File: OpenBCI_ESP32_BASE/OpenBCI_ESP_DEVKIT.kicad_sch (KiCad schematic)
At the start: 8 parts, among them J4 Conn_02x08_Odd_Even, U1 LIS3DH, U2 ESP32-DevKitC

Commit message: Firmware updates
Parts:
- added R3, R4: 4k7, Resistor_SMD:R_0603_1608Metric, symbol Device:R
- added R5: 220k, Resistor_SMD:R_0603_1608Metric, symbol Device:R
- added R6: 120k, Resistor_SMD:R_0603_1608Metric, symbol Device:R
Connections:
- net +3V3: now also R3.1, R4.1
- net +5V: now also R5.1
- net GND: now also R6.2
- net SCL: now also R4.2
- net SDA: now also R3.2
- net BATT: no longer names the net of U2.3 (SENSOR_VP/GPIO36/ADC1_CH0)
- net BATT: now also R5.2, R6.1
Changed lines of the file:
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@@
 (kicad_sch (version 20211123) (generator eeschema)
   (paper "A4")
+  (junction (at 68.58 57.15) (diameter 0) (color 0 0 0 0)
+  )
+  (junction (at 85.09 123.19) (diameter 0) (color 0 0 0 0)
+  )
   (junction (at 243.205 56.515) (diameter 0) (color 0 0 0 0)
   )
@@
   (junction (at 128.905 120.65) (diameter 0) (color 0 0 0 0)
   )
+  (junction (at 88.9 138.43) (diameter 0) (color 0 0 0 0)
+  )
   (junction (at 146.05 135.89) (diameter 0) (color 0 0 0 0)
+  )
+  (junction (at 82.55 135.89) (diameter 0) (color 0 0 0 0)
   )
   (no_connect (at 167.64 97.79))
@@
     (stroke (width 0) (type default) (color 0 0 0 0))
   )
+  (wire (pts (xy 68.58 67.31) (xy 68.58 71.12))
+    (stroke (width 0) (type default) (color 0 0 0 0))
+  )
   (wire (pts (xy 142.24 130.81) (xy 146.05 130.81))
     (stroke (width 0) (type default) (color 0 0 0 0))
@@
     (stroke (width 0) (type default) (color 0 0 0 0))
   )
+  (wire (pts (xy 85.09 120.65) (xy 85.09 123.19))
+    (stroke (width 0) (type default) (color 0 0 0 0))
+  )
   (wire (pts (xy 188.595 52.07) (xy 188.595 54.61))
     (stroke (width 0) (type default) (color 0 0 0 0))
   )
+  (wire (pts (xy 85.09 123.19) (xy 88.9 123.19))
+    (stroke (width 0) (type default) (color 0 0 0 0))
+  )
   (wire (pts (xy 213.36 74.93) (xy 223.52 74.93))
     (stroke (width 0) (type default) (color 0 0 0 0))
@@
     (stroke (width 0) (type default) (color 0 0 0 0))
   )
+  (wire (pts (xy 82.55 135.89) (xy 73.66 135.89))
+    (stroke (width 0) (type default) (color 0 0 0 0))
+  )
   (wire (pts (xy 86.36 77.47) (xy 97.79 77.47))
     (stroke (width 0) (type default) (color 0 0 0 0))
   )
+  (wire (pts (xy 88.9 132.08) (xy 88.9 138.43))
+    (stroke (width 0) (type default) (color 0 0 0 0))
+  )
   (wire (pts (xy 236.22 69.85) (xy 245.11 69.85))
     (stroke (width 0) (type default) (color 0 0 0 0))
@@
     (stroke (width 0) (type default) (color 0 0 0 0))
   )
+  (wire (pts (xy 88.9 123.19) (xy 88.9 124.46))
+    (stroke (width 0) (type default) (color 0 0 0 0))
+  )
   (wire (pts (xy 146.05 135.89) (xy 146.05 140.97))
     (stroke (width 0) (type default) (color 0 0 0 0))
@@
     (stroke (width 0) (type default) (color 0 0 0 0))
   )
-  (wire (pts (xy 97.79 57.15) (xy 85.09 57.15))
-    (stroke (width 0) (type default) (color 0 0 0 0))
-  )
   (wire (pts (xy 97.79 82.55) (xy 86.36 82.55))
     (stroke (width 0) (type default) (color 0 0 0 0))
@@
     (stroke (width 0) (type default) (color 0 0 0 0))
   )
-  (wire (pts (xy 116.84 135.89) (xy 98.425 135.89))
+  (wire (pts (xy 116.84 135.89) (xy 82.55 135.89))
     (stroke (width 0) (type default) (color 0 0 0 0))
   )
@@
     (stroke (width 0) (type default) (color 0 0 0 0))
   )
+  (wire (pts (xy 85.09 123.19) (xy 82.55 123.19))
+    (stroke (width 0) (type default) (color 0 0 0 0))
+  )
   (wire (pts (xy 241.3 80.01) (xy 241.3 81.915))
     (stroke (width 0) (type default) (color 0 0 0 0))
@@
     (stroke (width 0) (type default) (color 0 0 0 0))
   )
+  (wire (pts (xy 88.9 138.43) (xy 73.66 138.43))
+    (stroke (width 0) (type default) (color 0 0 0 0))
+  )
   (wire (pts (xy 129.54 148.59) (xy 129.54 156.21))
     (stroke (width 0) (type default) (color 0 0 0 0))
@@
     (stroke (width 0) (type default) (color 0 0 0 0))
   )
+  (wire (pts (xy 82.55 132.08) (xy 82.55 135.89))
+    (stroke (width 0) (type default) (color 0 0 0 0))
+  )
+  (wire (pts (xy 68.58 44.45) (xy 68.58 46.99))
+    (stroke (width 0) (type default) (color 0 0 0 0))
+  )
   (wire (pts (xy 225.425 111.125) (xy 225.425 110.49))
     (stroke (width 0) (type default) (color 0 0 0 0))
@@
     (stroke (width 0) (type default) (color 0 0 0 0))
   )
+  (wire (pts (xy 82.55 123.19) (xy 82.55 124.46))
+    (stroke (width 0) (type default) (color 0 0 0 0))
+  )
   (wire (pts (xy 201.295 140.335) (xy 192.405 140.335))
     (stroke (width 0) (type default) (color 0 0 0 0))
@@
     (stroke (width 0) (type default) (color 0 0 0 0))
   )
-  (wire (pts (xy 116.84 138.43) (xy 98.425 138.43))
+  (wire (pts (xy 68.58 57.15) (xy 68.58 59.69))
+    (stroke (width 0) (type default) (color 0 0 0 0))
+  )
+  (wire (pts (xy 68.58 54.61) (xy 68.58 57.15))
+    (stroke (width 0) (type default) (color 0 0 0 0))
+  )
+  (wire (pts (xy 68.58 57.15) (xy 97.79 57.15))
+    (stroke (width 0) (type default) (color 0 0 0 0))
+  )
+  (wire (pts (xy 116.84 138.43) (xy 88.9 138.43))
     (stroke (width 0) (type default) (color 0 0 0 0))
   )
@@
     (effects (font (size 1.27 1.27)) (justify right bottom))
   )
-  (label "BATT" (at 85.09 57.15 0)
-    (effects (font (size 1.27 1.27)) (justify left bottom))
-  )
   (label "SDCLK" (at 191.77 117.475 0)
     (effects (font (size 1.27 1.27)) (justify left bottom))
@@
     (effects (font (size 1.27 1.27)) (justify left bottom))
   )
-  (label "SCL" (at 98.425 138.43 0)
-    (effects (font (size 1.27 1.27)) (justify left bottom))
-  )
-  (label "SDA" (at 98.425 135.89 0)
+  (label "SCL" (at 73.66 138.43 0)
+    (effects (font (size 1.27 1.27)) (justify left bottom))
+  )
+  (label "SDA" (at 73.66 135.89 0)
     (effects (font (size 1.27 1.27)) (justify left bottom))
   )
@@
     (pin "1")
   )
+  (symbol (lib_id "Device:R") (at 88.9 128.27 0) (unit 1)
+    (in_bom yes) (on_board yes) (fields_autoplaced)
+    (property "Reference" "R4" (id 0) (at 90.678 127.3615 0)
+      (effects (font (size 1.27 1.27)) (justify left))
+    )
+    (property "Value" "4k7" (id 1) (at 90.678 130.1366 0)
+      (effects (font (size 1.27 1.27)) (justify left))
+    )
+    (property "Footprint" "Resistor_SMD:R_0603_1608Metric" (id 2) (at 87.122 128.27 90)
+      (effects (font (size 1.27 1.27)) hide)
+    )
+    (property "Datasheet" "~" (id 3) (at 88.9 128.27 0)
+      (effects (font (size 1.27 1.27)) hide)
+    )
+    (pin "1")
+    (pin "2")
+  )
+  (symbol (lib_id "power:+3.3V") (at 85.09 120.65 0) (unit 1)
+    (in_bom yes) (on_board yes)
+    (property "Reference" "#PWR0116" (id 0) (at 85.09 124.46 0)
+      (effects (font (size 1.27 1.27)) hide)
+    )
+    (property "Value" "+3.3V" (id 1) (at 85.471 116.2558 0))
+    (property "Footprint" "" (id 2) (at 85.09 120.65 0)
+      (effects (font (size 1.27 1.27)) hide)
+    )
+    (property "Datasheet" "" (id 3) (at 85.09 120.65 0)
+      (effects (font (size 1.27 1.27)) hide)
+    )
+    (pin "1")
+  )
+  (symbol (lib_id "power:GND") (at 68.58 71.12 0) (unit 1)
+    (in_bom yes) (on_board yes)
+    (property "Reference" "#PWR09" (id 0) (at 68.58 77.47 0)
+      (effects (font (size 1.27 1.27)) hide)
+    )
+    (property "Value" "GND" (id 1) (at 68.707 75.5142 0))
+    (property "Footprint" "" (id 2) (at 68.58 71.12 0)
+      (effects (font (size 1.27 1.27)) hide)
+    )
+    (property "Datasheet" "" (id 3) (at 68.58 71.12 0)
+      (effects (font (size 1.27 1.27)) hide)
+    )
+    (pin "1")
+  )
+  (symbol (lib_id "power:+5V") (at 68.58 44.45 0) (unit 1)
+    (in_bom yes) (on_board yes)
+    (property "Reference" "#PWR08" (id 0) (at 68.58 48.26 0)
+      (effects (font (size 1.27 1.27)) hide)
+    )
+    (property "Value" "+5V" (id 1) (at 68.961 40.0558 0))
+    (property "Footprint" "" (id 2) (at 68.58 44.45 0)
+      (effects (font (size 1.27 1.27)) hide)
+    )
+    (property "Datasheet" "" (id 3) (at 68.58 44.45 0)
+      (effects (font (size 1.27 1.27)) hide)
+    )
+    (pin "1")
+  )
+  (symbol (lib_id "Device:R") (at 68.58 63.5 0) (unit 1)
+    (in_bom yes) (on_board yes) (fields_autoplaced)
+    (property "Reference" "R6" (id 0) (at 70.358 62.5915 0)
+      (effects (font (size 1.27 1.27)) (justify left))
+    )
+    (property "Value" "120k" (id 1) (at 70.358 65.3666 0)
+      (effects (font (size 1.27 1.27)) (justify left))
+    )
+    (property "Footprint" "Resistor_SMD:R_0603_1608Metric" (id 2) (at 66.802 63.5 90)
+      (effects (font (size 1.27 1.27)) hide)
+    )
+    (property "Datasheet" "~" (id 3) (at 68.58 63.5 0)
+      (effects (font (size 1.27 1.27)) hide)
+    )
+    (pin "1")
+    (pin "2")
+  )
+  (symbol (lib_id "Device:R") (at 82.55 128.27 0) (unit 1)
+    (in_bom yes) (on_board yes) (fields_autoplaced)
+    (property "Reference" "R3" (id 0) (at 84.328 127.3615 0)
+      (effects (font (size 1.27 1.27)) (justify left))
+    )
+    (property "Value" "4k7" (id 1) (at 84.328 130.1366 0)
+      (effects (font (size 1.27 1.27)) (justify left))
+    )
+    (property "Footprint" "Resistor_SMD:R_0603_1608Metric" (id 2) (at 80.772 128.27 90)
+      (effects (font (size 1.27 1.27)) hide)
+    )
+    (property "Datasheet" "~" (id 3) (at 82.55 128.27 0)
+      (effects (font (size 1.27 1.27)) hide)
+    )
+    (pin "1")
+    (pin "2")
+  )
+  (symbol (lib_id "Device:R") (at 68.58 50.8 0) (unit 1)
+    (in_bom yes) (on_board yes) (fields_autoplaced)
+    (property "Reference" "R5" (id 0) (at 70.358 49.8915 0)
+      (effects (font (size 1.27 1.27)) (justify left))
+    )
+    (property "Value" "220k" (id 1) (at 70.358 52.6666 0)
+      (effects (font (size 1.27 1.27)) (justify left))
+    )
+    (property "Footprint" "Resistor_SMD:R_0603_1608Metric" (id 2) (at 66.802 50.8 90)
+      (effects (font (size 1.27 1.27)) hide)
+    )
+    (property "Datasheet" "~" (id 3) (at 68.58 50.8 0)
+      (effects (font (size 1.27 1.27)) hide)
+    )
+    (pin "1")
+    (pin "2")
+  )
 )

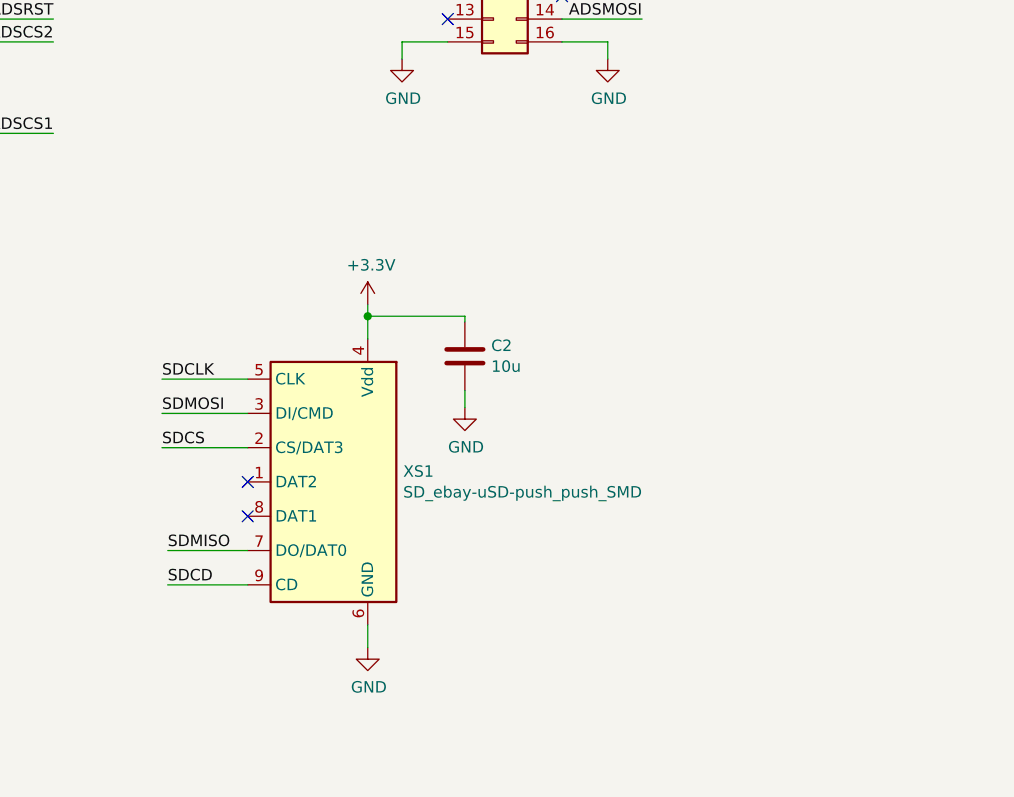
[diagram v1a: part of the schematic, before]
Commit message: Kicad and firmware updates
Kicad schematic and PCB updates for SD Card issue
Firmware tests for SD card
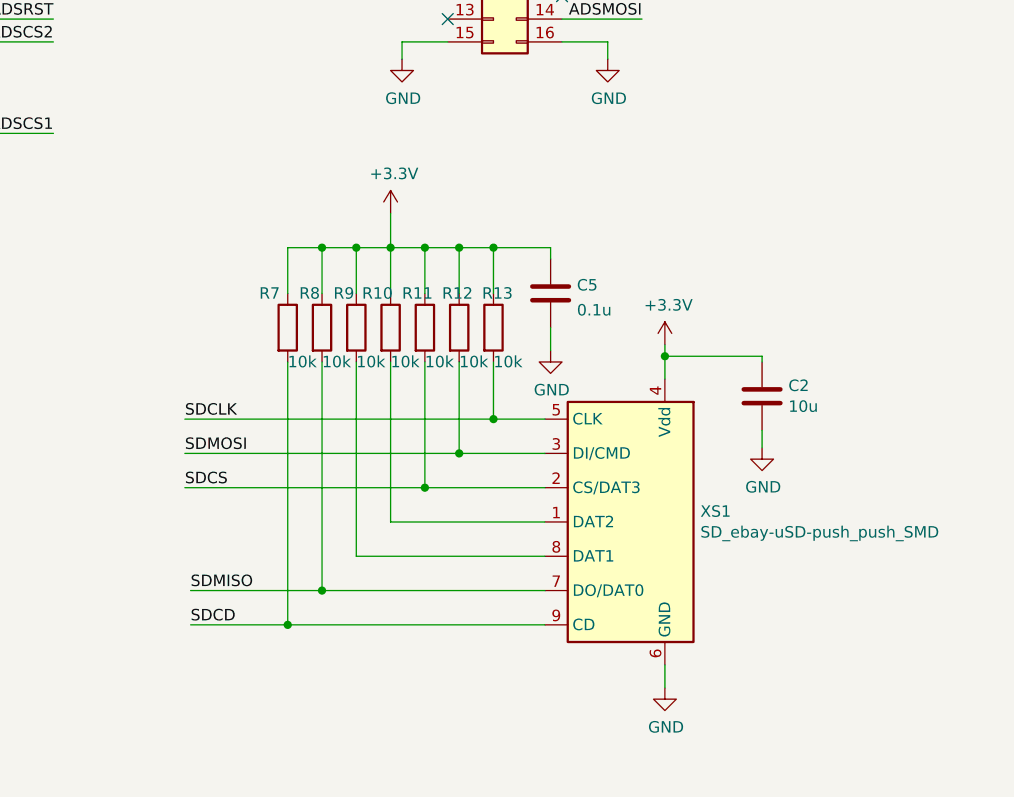
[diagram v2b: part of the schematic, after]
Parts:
- added C5: 0.1u, Capacitor_SMD:C_0603_1608Metric, symbol Device:C
- added R10, R11, R12, R13, R7, R8, R9: 10k, Resistor_SMD:R_0603_1608Metric, symbol Device:R
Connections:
- net +3V3: now also C5.1, R10.1, R11.1, R12.1, R13.1, R7.1, R8.1, R9.1
- net GND: now also C5.2
- net SDCD: now also R7.2
- net SDCLK: now also R13.2
- net SDCS: now also R11.2
- net SDMISO: now also R8.2
- net SDMOSI: now also R12.2
- net at XS1.1 (DAT2): now also R10.2
- net at XS1.8 (DAT1): now also R9.2
- no-connect marks 24 -> 22
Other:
- moved on the sheet: C2, XS1

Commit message: Code and STL updates
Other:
- moved on the sheet: C3, J4, R5, R6, U2

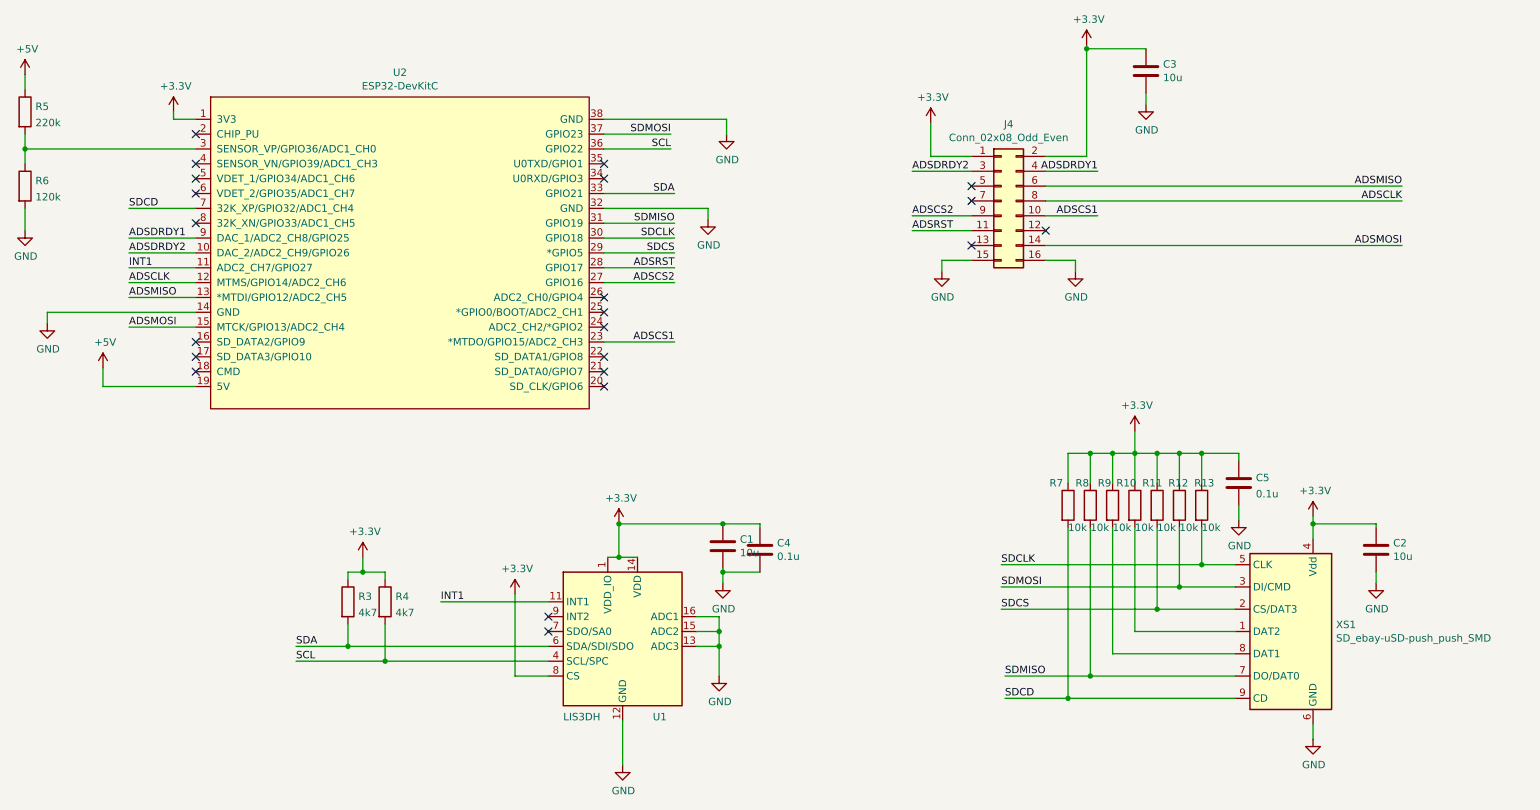
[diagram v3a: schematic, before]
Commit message: add ADS1298 files
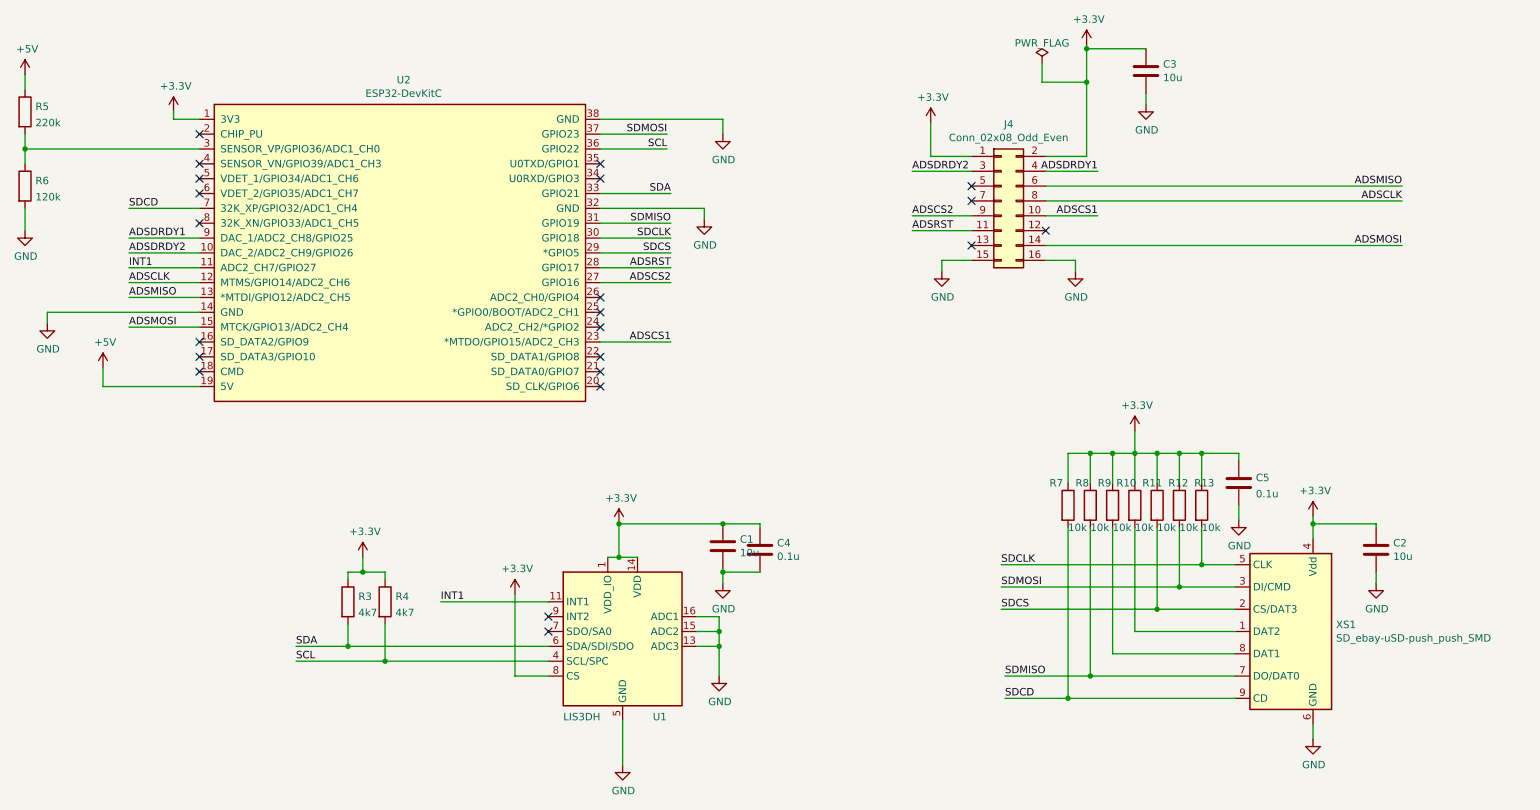
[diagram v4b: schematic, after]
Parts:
- U2: footprint OpenBCI_ESP32:ESP32-DevKitC -> Espressif:ESP32-DevKitC
- XS1: footprint OpenBCI_ESP32:Conn_uSDcard -> Connectors:Conn_uSDcard
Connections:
- net +3V3 renamed +3.3V
